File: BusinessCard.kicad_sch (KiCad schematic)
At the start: 177 parts, among them J1 Conn_01x03_Socket, J2 Conn_01x04_Socket, J3 Conn_01x02, SW1 Up, SW2 Left, SW3 Down, SW4 Right, SW5 A, SW6 B, U1 STM32F103C8T6

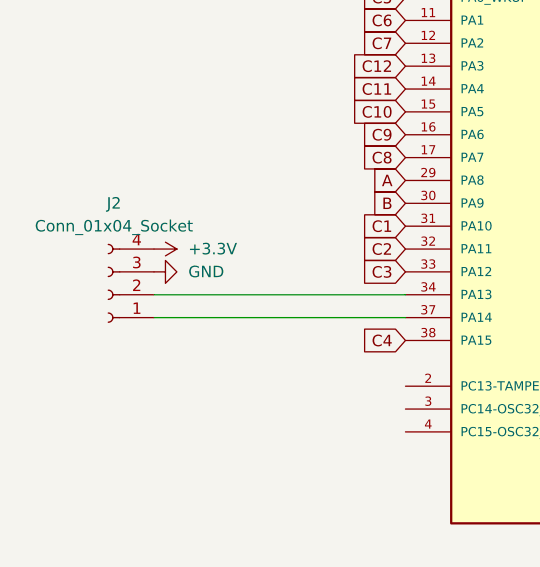
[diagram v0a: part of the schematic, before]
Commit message: Rearranged back and added KiCad logo
- Rearranged back to avoid via collision
- Added KiCad logo
- Moved some via's for cleanliness
- Moved keychain hole label position
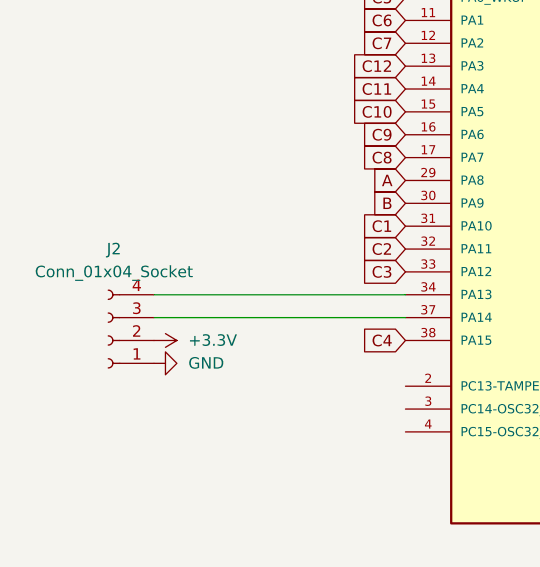
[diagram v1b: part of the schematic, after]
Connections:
- net +3.3V: now also J2.2 (Pin_2); no longer J2.4 (Pin_4)
- net GND: now also J2.1 (Pin_1); no longer J2.3 (Pin_3)
- net at U1.34 (PA13): now also J2.4 (Pin_4); no longer J2.2 (Pin_2)
- net at U1.37 (PA14): now also J2.3 (Pin_3); no longer J2.1 (Pin_1)
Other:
- moved on the sheet: J2
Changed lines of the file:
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@@
 	(symbol
 		(lib_id "power:+3.3V")
-		(at 58.42 128.27 270)
+		(at 58.42 138.43 270)
 		(unit 1)
 		(exclude_from_sim no)
@@
 		(fields_autoplaced yes)
 		(property "Reference" "#PWR04"
-			(at 54.61 128.27 0)
+			(at 54.61 138.43 0)
 			(effects
 				(font
@@
 		)
 		(property "Value" "+3.3V"
-			(at 62.23 128.2699 90)
+			(at 62.23 138.4299 90)
 			(effects
 				(font
@@
 		)
 		(property "Footprint" ""
-			(at 58.42 128.27 0)
+			(at 58.42 138.43 0)
 			(effects
 				(font
@@
 		)
 		(property "Datasheet" ""
-			(at 58.42 128.27 0)
+			(at 58.42 138.43 0)
 			(effects
 				(font
@@
 		)
 		(property "Description" "Power symbol creates a global label with name \"+3.3V\""
-			(at 58.42 128.27 0)
+			(at 58.42 138.43 0)
 			(effects
 				(font
@@
 	(symbol
 		(lib_id "Connector:Conn_01x04_Socket")
-		(at 53.34 133.35 180)
+		(at 53.34 138.43 180)
 		(unit 1)
 		(exclude_from_sim no)
@@
 		(fields_autoplaced yes)
 		(property "Reference" "J2"
-			(at 53.975 123.19 0)
+			(at 53.975 128.27 0)
 			(effects
 				(font
@@
 		)
 		(property "Value" "Conn_01x04_Socket"
-			(at 53.975 125.73 0)
+			(at 53.975 130.81 0)
 			(effects
 				(font
@@
 		)
 		(property "Footprint" "Dependencies:RoundSolderPad_1x4_1mm"
-			(at 53.34 133.35 0)
+			(at 53.34 138.43 0)
 			(effects
 				(font
@@
 		)
 		(property "Datasheet" "~"
-			(at 53.34 133.35 0)
+			(at 53.34 138.43 0)
 			(effects
 				(font
@@
 		)
 		(property "Description" "Generic connector, single row, 01x04, script generated"
-			(at 53.34 133.35 0)
+			(at 53.34 138.43 0)
 			(effects
 				(font
@@
 		)
 		(instances
-			(project ""
+			(project "BusinessCard"
 				(path "/e6903c3c-d24e-4d4a-96bc-6632eb326ff1"
 					(reference "J2")
@@
 	(symbol
 		(lib_id "power:GND")
-		(at 58.42 130.81 90)
+		(at 58.42 140.97 90)
 		(unit 1)
 		(exclude_from_sim no)
@@
 		(fields_autoplaced yes)
 		(property "Reference" "#PWR03"
-			(at 64.77 130.81 0)
+			(at 64.77 140.97 0)
 			(effects
 				(font
@@
 		)
 		(property "Value" "GND"
-			(at 62.23 130.8099 90)
+			(at 62.23 140.9699 90)
 			(effects
 				(font
@@
 		)
 		(property "Footprint" ""
-			(at 58.42 130.81 0)
+			(at 58.42 140.97 0)
 			(effects
 				(font
@@
 		)
 		(property "Datasheet" ""
-			(at 58.42 130.81 0)
+			(at 58.42 140.97 0)
 			(effects
 				(font
@@
 		)
 		(property "Description" "Power symbol creates a global label with name \"GND\" , ground"
-			(at 58.42 130.81 0)
+			(at 58.42 140.97 0)
 			(effects
 				(font

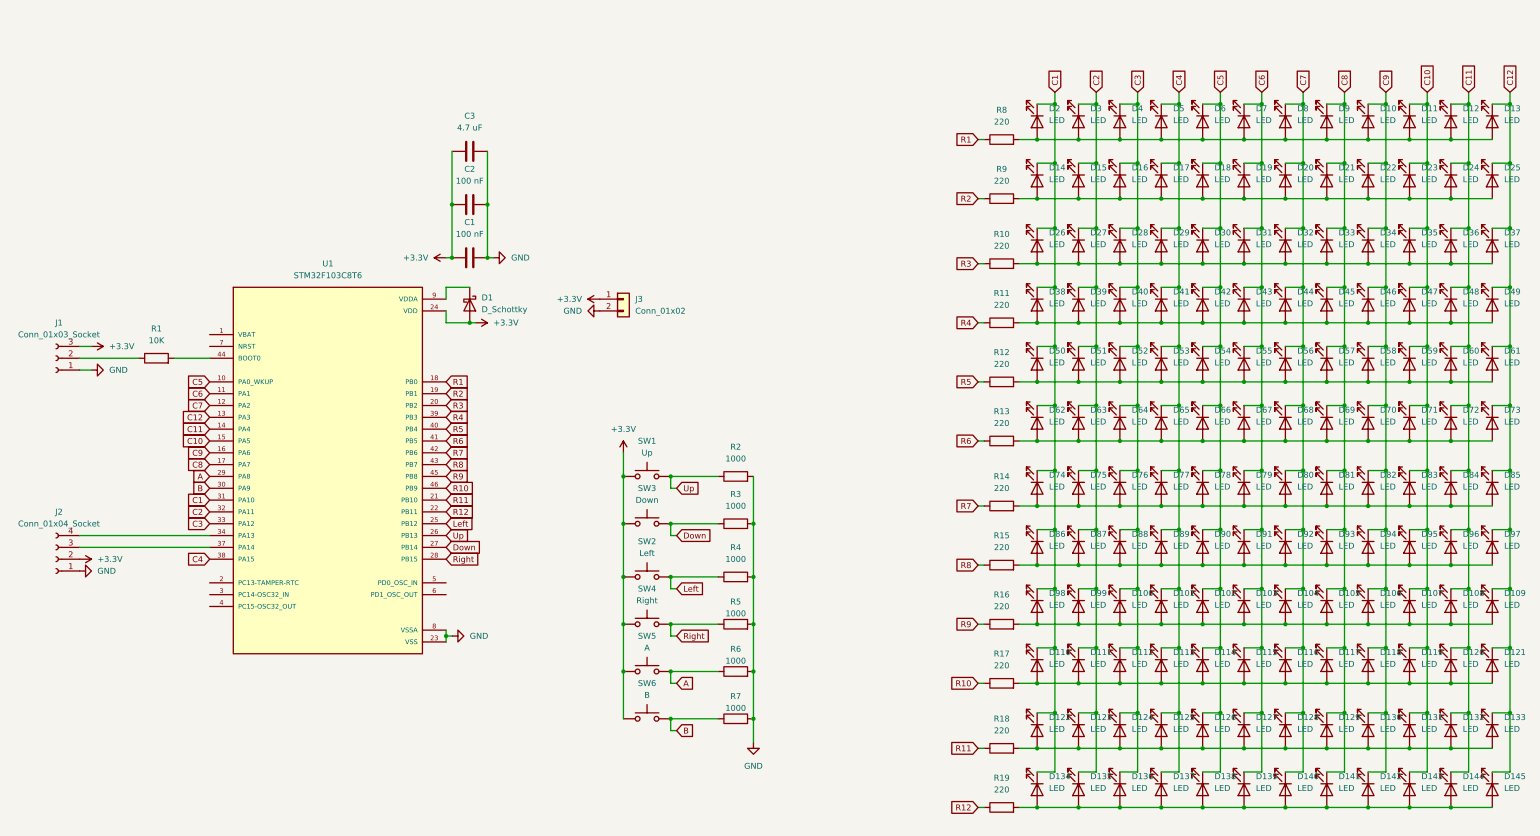
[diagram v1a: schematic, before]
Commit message: Fabrication edits
- Added JLCPCB component part numbers
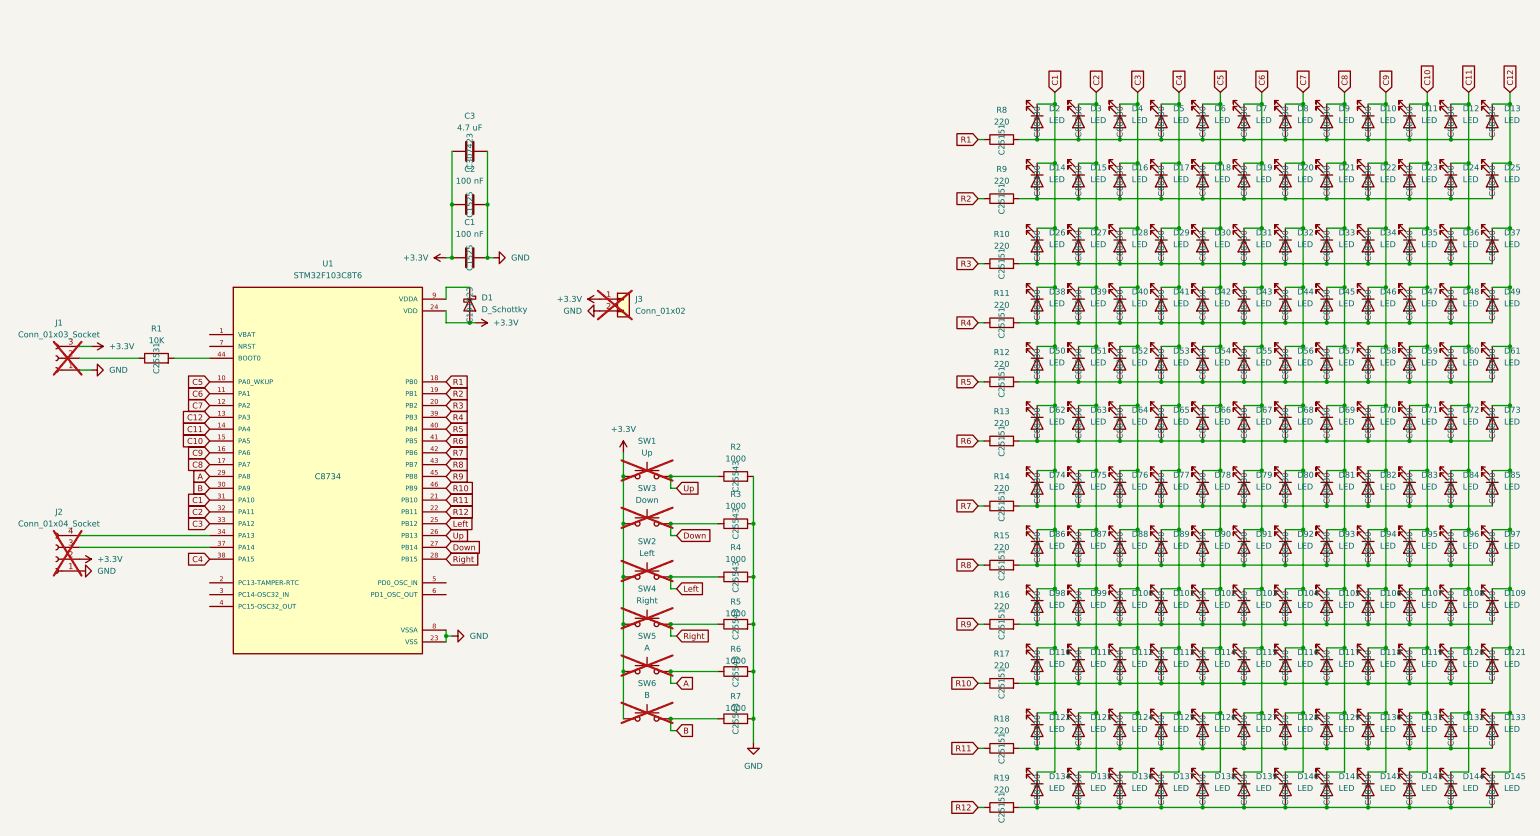
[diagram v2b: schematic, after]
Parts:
- C1, C2: LCSC (none) -> C1525
- C3: LCSC (none) -> C307423
- D1: LCSC (none) -> C191023
- D10, D100, D101, D102, D103, D104, D105, D106, D107, D108, D109, D11, D110, D111, D112, D113, D114, D115, D116, D117, D118, D119, D12, D120, D121, D122, D123, D124, D125, D126, D127, D128, D129, D13, D130, D131, D132, D133, D134, D135, D136, D137, D138, D139, D14, D140, D141, D142, D143, D144, D145, D15, D16, D17, D18, D19, D2, D20, D21, D22, D23, D24, D25, D26, D27, D28, D29, D3, D30, D31, D32, D33, D34, D35, D36, D37, D38, D39, D4, D40, D41, D42, D43, D44, D45, D46, D47, D48, D49, D5, D50, D51, D52, D53, D54, D55, D56, D57, D58, D59, D6, D60, D61, D62, D63, D64, D65, D66, D67, D68, D69, D7, D70, D71, D72, D73, D74, D75, D76, D77, D78, D79, D8, D80, D81, D82, D83, D84, D85, D86, D87, D88, D89, D9, D90, D91, D92, D93, D94, D95, D96, D97, D98, D99: LCSC (none) -> C88330
- J1, J2, J3, SW1, SW2, SW3, SW4, SW5, SW6: now not fitted; now left out of the parts list
- R1: LCSC (none) -> C25531
- R10, R11, R12, R13, R14, R15, R16, R17, R18, R19, R8, R9: LCSC (none) -> C25151
- R2, R3, R4, R5, R6, R7: LCSC (none) -> C25543
- U1: LCSC (none) -> C8734

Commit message: Switched LED footprint and fixed row traces
- Switched LED footprints from 0402 to 0603 to reduce assembly cost
- Added back row traces that were accidentally removed in an earlier commit
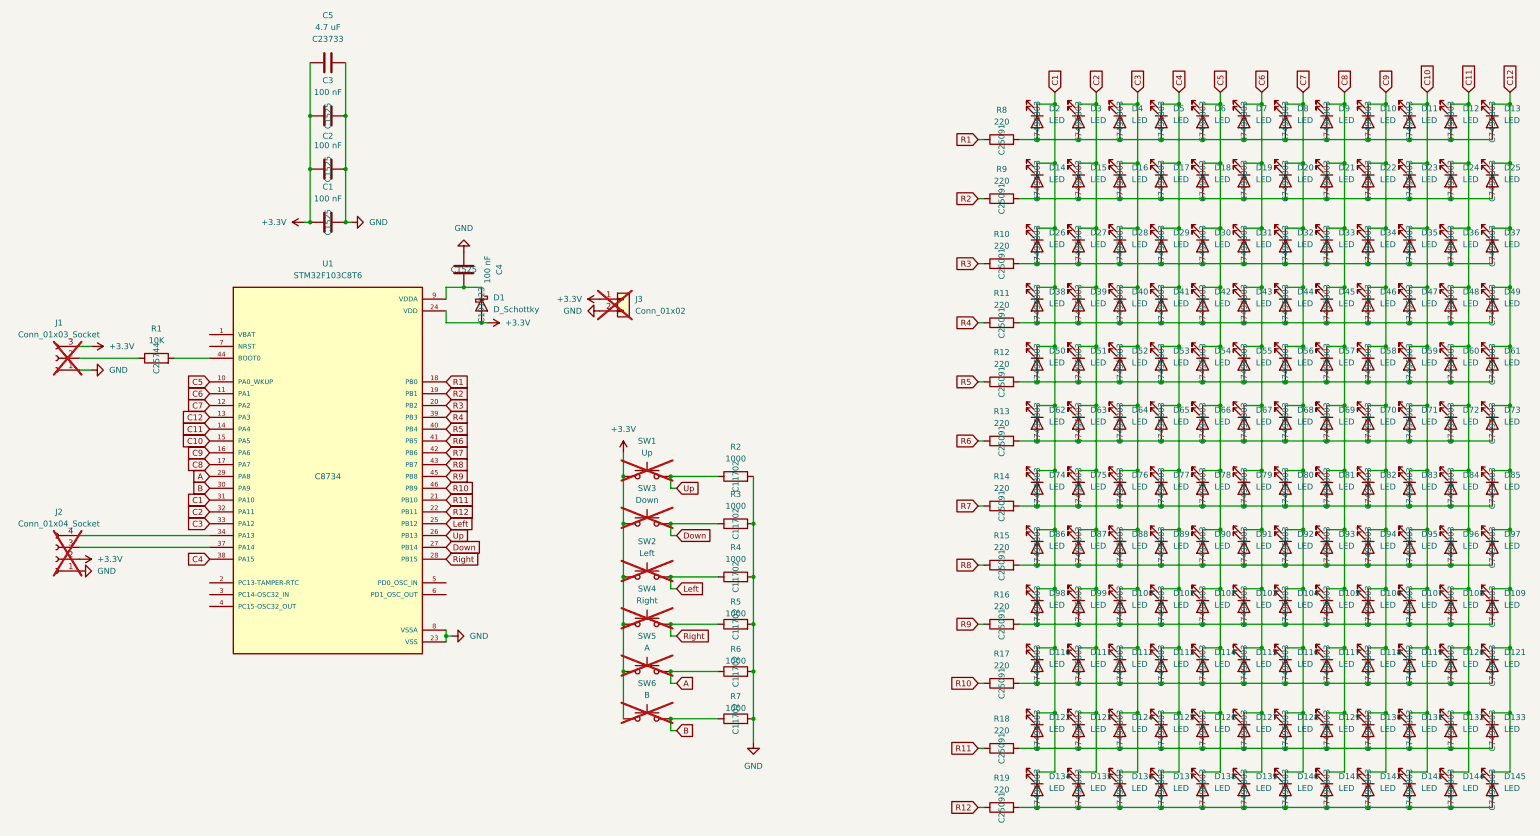
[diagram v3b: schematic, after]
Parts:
- added C3, C4: 100 nF, Capacitor_SMD:C_0402_1005Metric_Pad0.74x0.62mm_HandSolder, symbol Device:C
- C5: renamed from C3; LCSC C307423 -> C23733
- D10, D100, D101, D102, D103, D104, D105, D106, D107, D108, D109, D11, D110, D111, D112, D113, D114, D115, D116, D117, D118, D119, D12, D120, D121, D122, D123, D124, D125, D126, D127, D128, D129, D13, D130, D131, D132, D133, D134, D135, D136, D137, D138, D139, D14, D140, D141, D142, D143, D144, D145, D15, D16, D17, D18, D19, D2, D20, D21, D22, D23, D24, D25, D26, D27, D28, D29, D3, D30, D31, D32, D33, D34, D35, D36, D37, D38, D39, D4, D40, D41, D42, D43, D44, D45, D46, D47, D48, D49, D5, D50, D51, D52, D53, D54, D55, D56, D57, D58, D59, D6, D60, D61, D62, D63, D64, D65, D66, D67, D68, D69, D7, D70, D71, D72, D73, D74, D75, D76, D77, D78, D79, D8, D80, D81, D82, D83, D84, D85, D86, D87, D88, D89, D9, D90, D91, D92, D93, D94, D95, D96, D97, D98, D99: footprint Dependencies:LED_0402_1005Metric_Pad0.77x0.64mm_HandSolder_Notext -> Dependencies:LED_0603_1608Metric_Notext; LCSC C88330 -> C7496803
- R1: LCSC C25531 -> C25744
- R10, R11, R12, R13, R14, R15, R16, R17, R18, R19, R8, R9: LCSC C25151 -> C25091
- R2, R3, R4, R5, R6, R7: LCSC C25543 -> C11702
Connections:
- net +3.3V: now also C3.1
- net GND: now also C3.2, C4.1
- net at D1.1 (K), U1.9 (VDDA): now also C4.2
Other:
- moved on the sheet: C1, C2, C5, D1
